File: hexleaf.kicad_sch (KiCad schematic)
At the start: 41 parts, among them IC1 ESP32-C3-FH4, J2 Conn_01x04, J5 Conn_01x08, J6 Conn_01x04, J7 Conn_01x08, SW1 SW_SPST, SW2 SW_SPST, Y1 ECS-400-10-37B2-CKM-TR

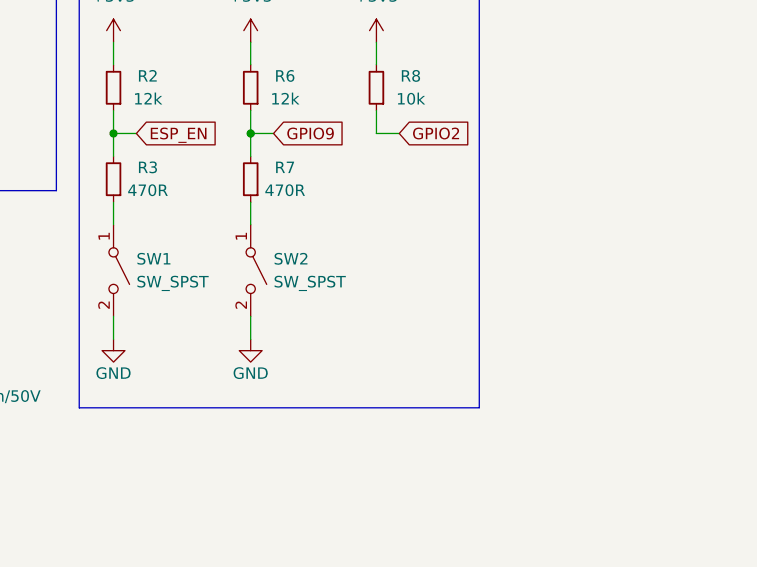
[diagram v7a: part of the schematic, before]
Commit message: added strapping pin
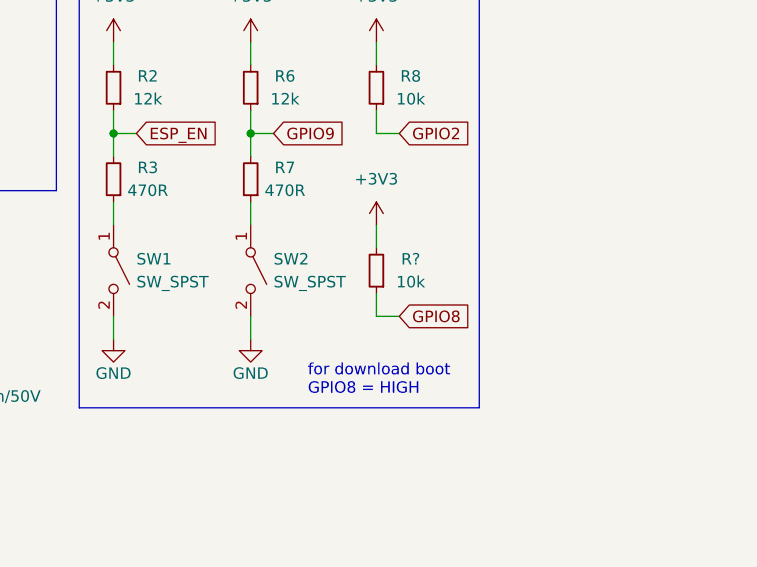
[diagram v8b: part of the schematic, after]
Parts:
- added R?: 10k, Resistor_SMD:R_0805_2012Metric, symbol Device:R_Small
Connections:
- net +3V3: now also R?.2
- new net GPIO8: R?.1
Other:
- note added: "for download boot GPIO8 = HIGH"
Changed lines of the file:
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@@
+    (stroke (width 0) (type default) (color 0 0 0 0))
+  )
+  (wire (pts (xy 293.37 130.81) (xy 293.37 133.35))
     (stroke (width 0) (type default) (color 0 0 0 0))
   )
@@
     (stroke (width 0) (type default) (color 0 0 0 0))
   )
+  (wire (pts (xy 293.37 138.43) (xy 293.37 140.97))
+    (stroke (width 0) (type default) (color 0 0 0 0))
+  )
   (wire (pts (xy 274.32 45.72) (xy 276.86 45.72))
     (stroke (width 0) (type default) (color 0 0 0 0))
@@
   )
   (wire (pts (xy 64.77 123.19) (xy 64.77 125.73))
+    (stroke (width 0) (type default) (color 0 0 0 0))
+  )
+  (wire (pts (xy 295.91 140.97) (xy 293.37 140.97))
     (stroke (width 0) (type default) (color 0 0 0 0))
   )
@@
   )
   (text "Board to strip connector" (at 123.19 137.16 0)
+    (effects (font (size 1.27 1.27)) (justify left bottom))
+  )
+  (text "for download boot\nGPIO8 = HIGH" (at 285.75 149.86 0)
     (effects (font (size 1.27 1.27)) (justify left bottom))
   )
@@
     )
   )
+  (global_label "GPIO8" (shape input) (at 295.91 140.97 0) (fields_autoplaced)
+    (effects (font (size 1.27 1.27)) (justify left))
+    (property "Intersheet References" "${INTERSHEET_REFS}" (id 0) (at 303.919 140.8906 0)
+      (effects (font (size 1.27 1.27)) (justify left) hide)
+    )
+  )
   (global_label "VCC_RTC" (shape input) (at 99.06 69.85 0) (fields_autoplaced)
     (effects (font (size 1.27 1.27)) (justify left))
@@
     )
     (pin "1")
+  )
+  (symbol (lib_id "Device:R_Small") (at 293.37 135.89 180) (unit 1)
+    (in_bom yes) (on_board yes)
+    (property "Reference" "R?" (id 0) (at 297.18 134.62 0))
+    (property "Value" "10k" (id 1) (at 297.18 137.16 0))
+    (property "Footprint" "Resistor_SMD:R_0805_2012Metric" (id 2) (at 293.37 135.89 0)
+      (effects (font (size 1.27 1.27)) hide)
+    )
+    (property "Datasheet" "https://www.mouser.de/datasheet/2/418/4/NG_DS_1773204-3_1-1358553.pdf" (id 3) (at 293.37 135.89 0)
+      (effects (font (size 1.27 1.27)) hide)
+    )
+    (property "MFN" " 279-CRGCQ0805F10K " (id 4) (at 293.37 135.89 0)
+      (effects (font (size 1.27 1.27)) hide)
+    )
+    (pin "1")
+    (pin "2")
   )
   (symbol (lib_id "Connector_Generic:Conn_01x04") (at 147.32 149.86 0) (unit 1)
@@
     (pin "2")
   )
+  (symbol (lib_id "power:+3V3") (at 293.37 130.81 0) (unit 1)
+    (in_bom yes) (on_board yes) (fields_autoplaced)
+    (property "Reference" "#PWR?" (id 0) (at 293.37 134.62 0)
+      (effects (font (size 1.27 1.27)) hide)
+    )
+    (property "Value" "+3V3" (id 1) (at 293.37 125.73 0))
+    (property "Footprint" "" (id 2) (at 293.37 130.81 0)
+      (effects (font (size 1.27 1.27)) hide)
+    )
+    (property "Datasheet" "" (id 3) (at 293.37 130.81 0)
+      (effects (font (size 1.27 1.27)) hide)
+    )
+    (pin "1")
+  )
   (symbol (lib_id "Device:C_Small") (at 96.52 44.45 0) (unit 1)
     (in_bom yes) (on_board yes)
@@
       (reference "#PWR?") (unit 1) (value "GND") (footprint "")
     )
+    (path "/bf714755-9f15-4161-aa34-ebb85baa5742"
+      (reference "#PWR?") (unit 1) (value "+3V3") (footprint "")
+    )
     (path "/716330f7-8bae-4a6f-9b80-4a183d97132d"
       (reference "ANT1") (unit 1) (value "AMCA31-2R450G-S1F-T3") (footprint "hexleaf:ANTC3216X140N")
@@
       (reference "R8") (unit 1) (value "10k") (footprint "Resistor_SMD:R_0805_2012Metric")
     )
+    (path "/0a517b9a-a9fc-44f0-b6e1-5b5bad5d4c74"
+      (reference "R?") (unit 1) (value "10k") (footprint "Resistor_SMD:R_0805_2012Metric")
+    )
     (path "/508cc352-4d19-4358-95ba-715645cd1a5a"
